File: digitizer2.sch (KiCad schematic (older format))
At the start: 4 parts, among them U1 XC7A35T, U2 FT2232H, U3 MT41K128M16, U4 ADS5403

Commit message: .
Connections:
- net labels added: ADC_DA0_N, ADC_DA0_P, ADC_DA10_N, ADC_DA10_P, ADC_DA11_N, ADC_DA11_P, ADC_DA1_N, ADC_DA1_P, ADC_DA2_N, ADC_DA2_P, ADC_DA3_N, ADC_DA3_P, ADC_DA4_N, ADC_DA4_P, ADC_DA5_N, ADC_DA5_P, ADC_DA6_N, ADC_DA6_P, ADC_DA7_N, ADC_DA7_P, ADC_DA8_N, ADC_DA8_P, ADC_DA9_N, ADC_DA9_P, ADC_DACLK_N, ADC_DACLK_P, ADC_OVRA_N, ADC_OVRA_P, ADC_SCLK, ADC_SDENB, ADC_SDIO, ADC_SDO, DRAM_A0, DRAM_A1, DRAM_A10, DRAM_A11, DRAM_A12, DRAM_A13, DRAM_A2, DRAM_A3, DRAM_A4, DRAM_A5, DRAM_A6, DRAM_A7, DRAM_A8, DRAM_A9, DRAM_BA0, DRAM_BA1, DRAM_BA2, DRAM_CAS, DRAM_CKE, DRAM_CK_N, DRAM_CK_P, DRAM_CS, DRAM_DM0, DRAM_DM1, DRAM_DQ0, DRAM_DQ1, DRAM_DQ10, DRAM_DQ11, DRAM_DQ12, DRAM_DQ13, DRAM_DQ14, DRAM_DQ15, DRAM_DQ2, DRAM_DQ3, DRAM_DQ4, DRAM_DQ5, DRAM_DQ6, DRAM_DQ7, DRAM_DQ8, DRAM_DQ9, DRAM_DQS0_N, DRAM_DQS0_P, DRAM_DQS1_N, DRAM_DQS1_P, DRAM_ODT, DRAM_RAS, DRAM_RESET, DRAM_WE, DRAM_ZQ, JTAG_TCK, JTAG_TDI, JTAG_TDO, JTAG_TMS, USB_CLKOUT, USB_D0, USB_D1, USB_D2, USB_D3, USB_D4, USB_D5, USB_D6, USB_D7, USB_OE, USB_RD, USB_RXF, USB_TXE, USB_WR
- wire segments 8 -> 18
- no-connect marks 0 -> 19
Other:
- moved on the sheet: U4

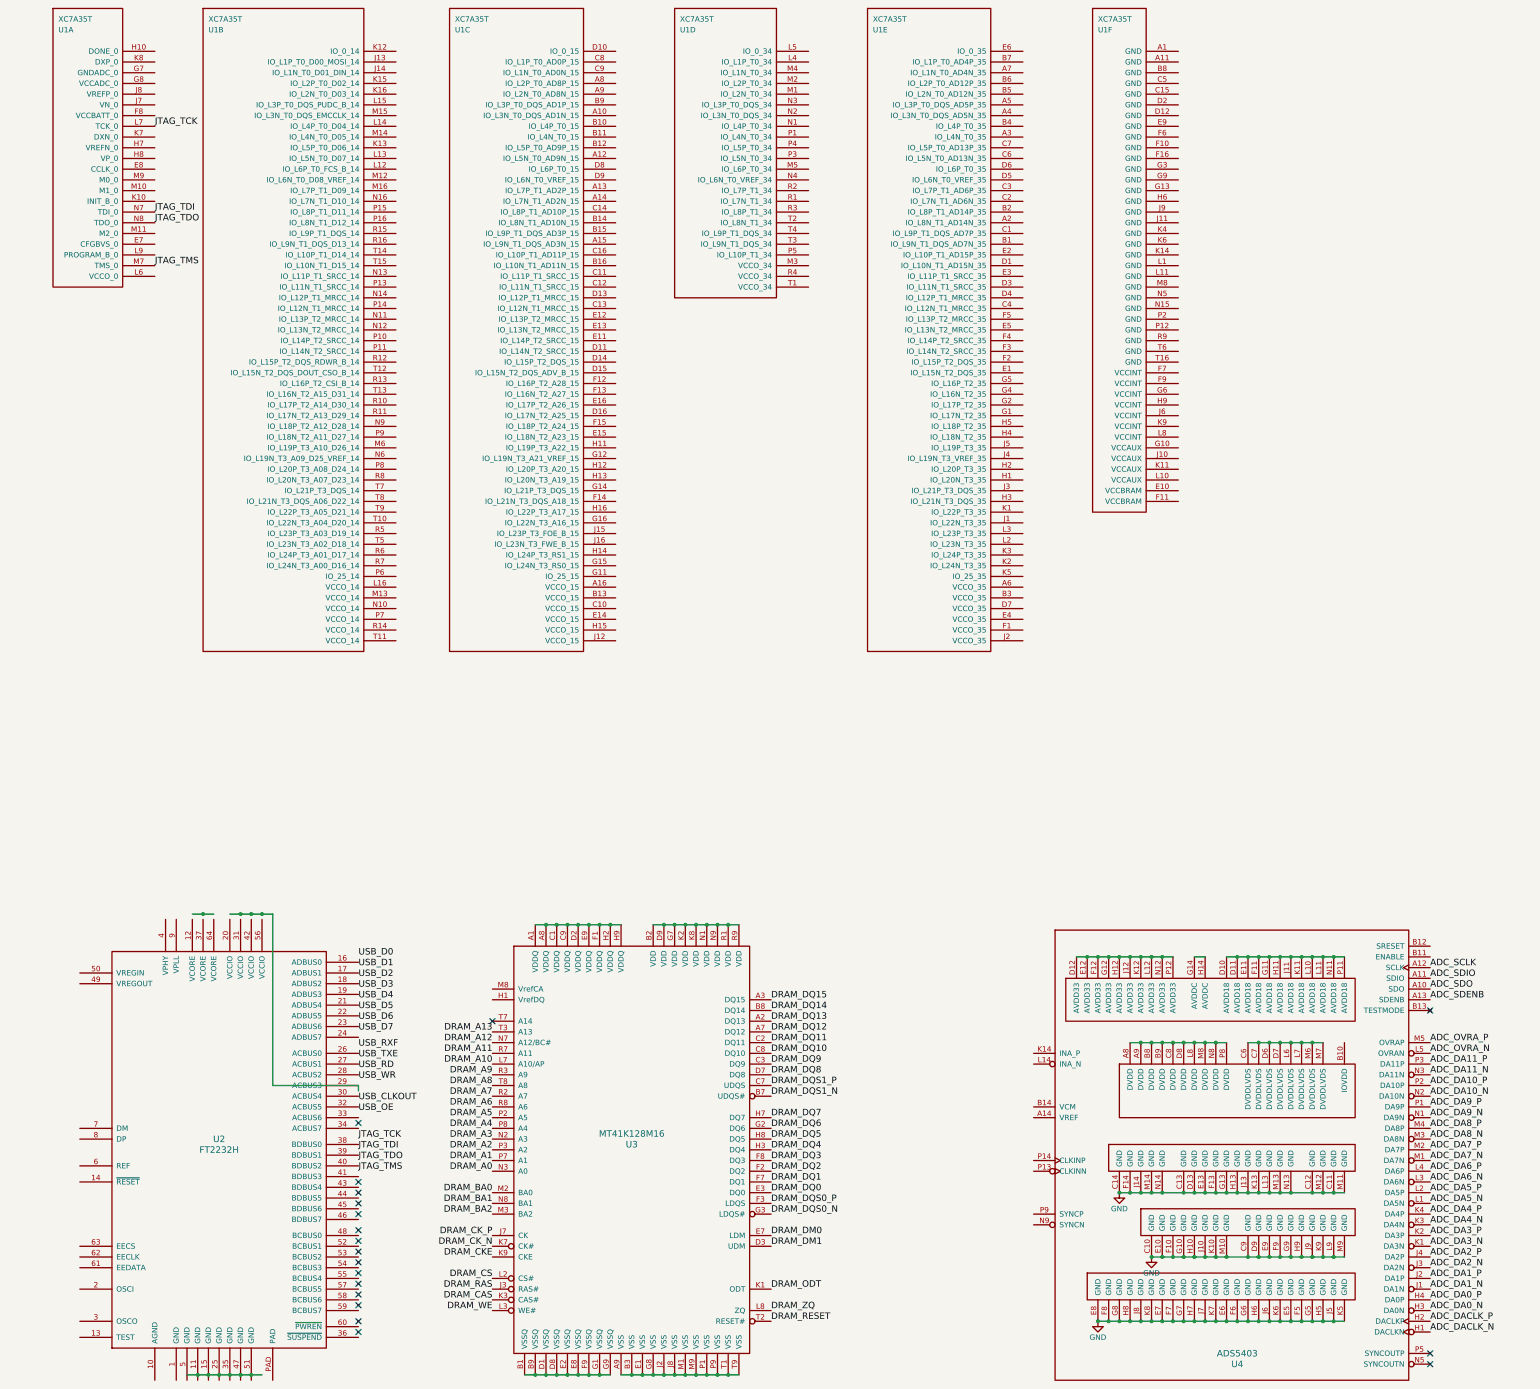
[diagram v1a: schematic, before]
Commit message: Tuned ADC DDR layout
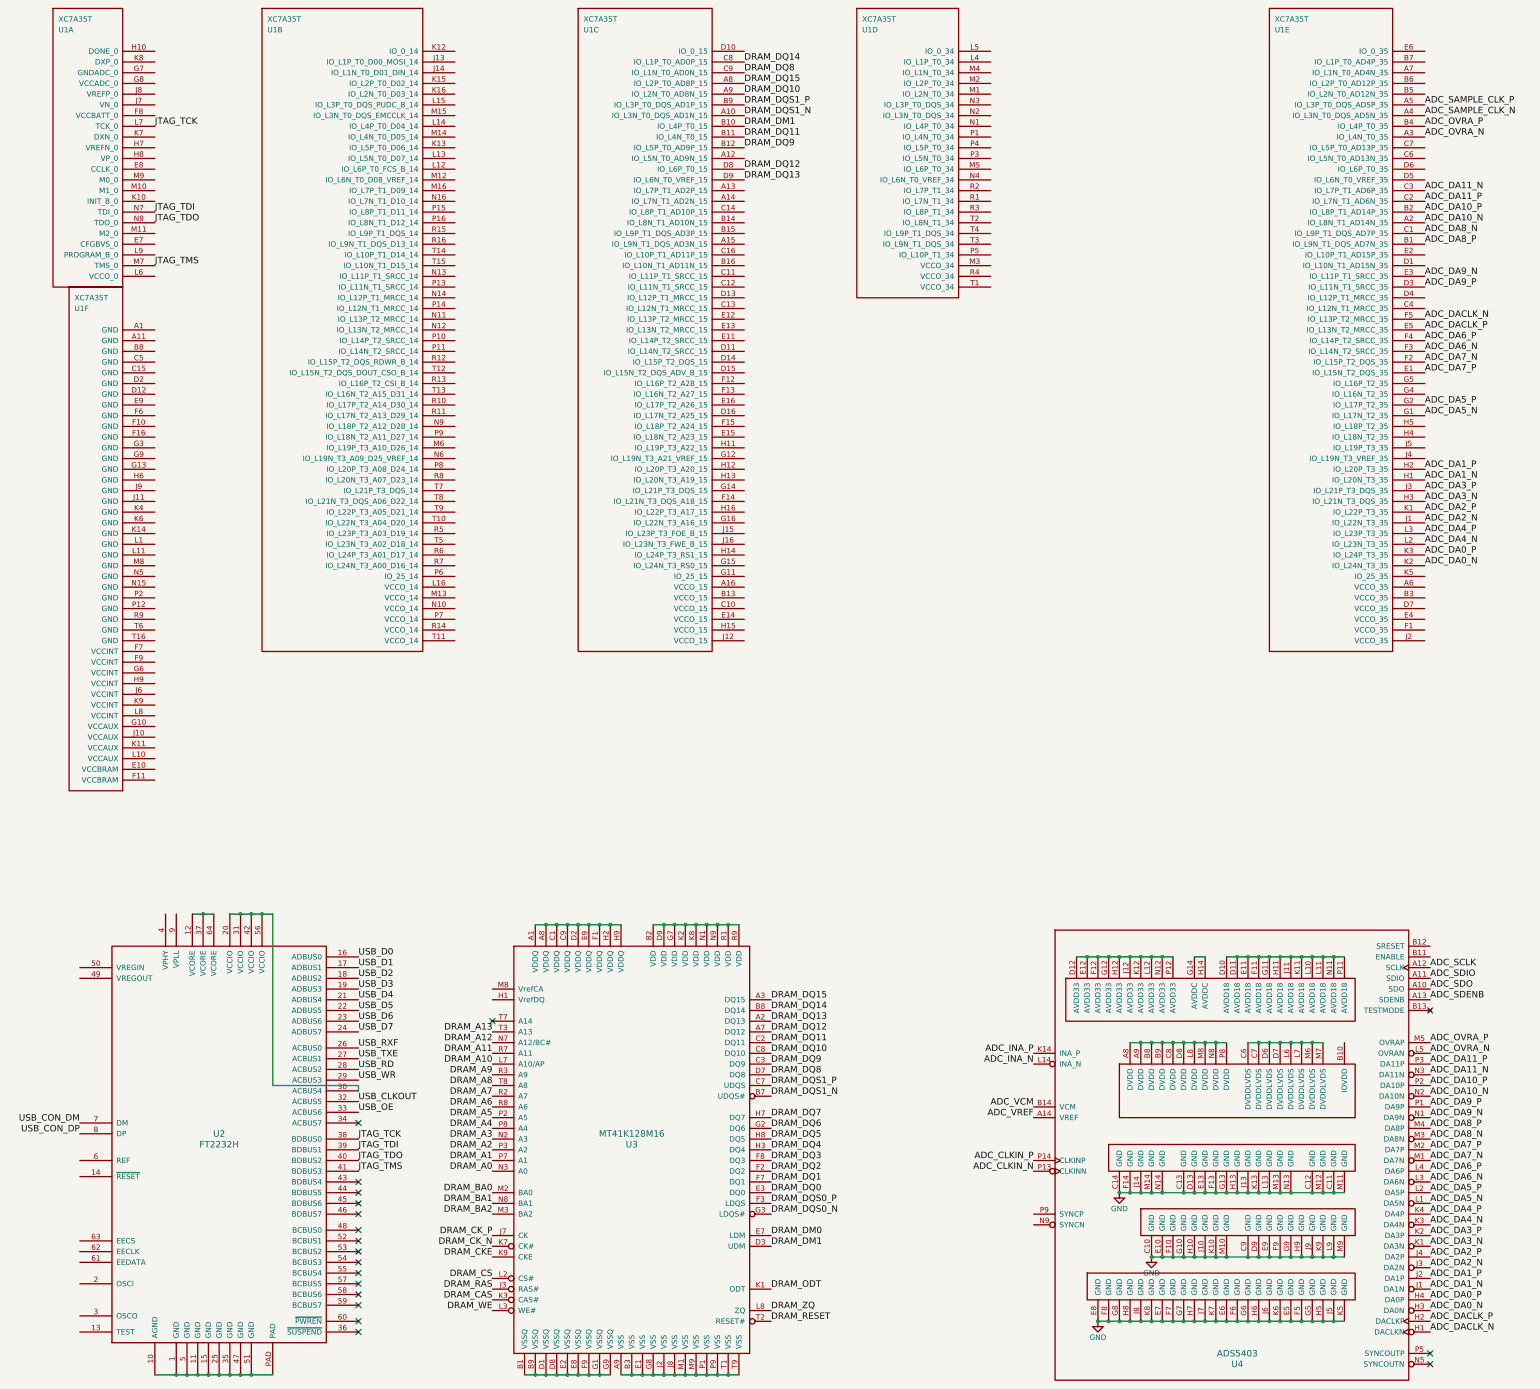
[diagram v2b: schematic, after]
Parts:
- U2: footprint (none) -> digitizer2_modules:QFN-FT2232HQ-64_pitch0.5
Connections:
- net labels added: ADC_CLKIN_N, ADC_CLKIN_P, ADC_INA_N, ADC_INA_P, ADC_SAMPLE_CLK_N, ADC_SAMPLE_CLK_P, ADC_VCM, ADC_VREF, USB_CON_DM, USB_CON_DP
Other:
- moved on the sheet: U1B, U1C, U1D, U1E, U1F, U2
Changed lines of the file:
@@
 L XC7A35T U1
 U 2 1 56D56ABF
-P 1900 800
-F 0 "U1" H 1950 900 50  0000 L CNN
-F 1 "XC7A35T" H 1950 1000 50  0000 L CNN
-F 2 "" H 1900 800 60  0000 C CNN
-F 3 "" H 1900 800 60  0000 C CNN
-	2    1900 800
+P 2450 800
+F 0 "U1" H 2500 900 50  0000 L CNN
+F 1 "XC7A35T" H 2500 1000 50  0000 L CNN
+F 2 "" H 2450 800 60  0000 C CNN
+F 3 "" H 2450 800 60  0000 C CNN
+	2    2450 800
 	1    0    0    -1
 $EndComp
@@
 L XC7A35T U1
 U 3 1 56D56B34
-P 4200 800
-F 0 "U1" H 4250 900 50  0000 L CNN
-F 1 "XC7A35T" H 4250 1000 50  0000 L CNN
-F 2 "" H 4200 800 60  0000 C CNN
-F 3 "" H 4200 800 60  0000 C CNN
-	3    4200 800
+P 5400 800
+F 0 "U1" H 5450 900 50  0000 L CNN
+F 1 "XC7A35T" H 5450 1000 50  0000 L CNN
+F 2 "" H 5400 800 60  0000 C CNN
+F 3 "" H 5400 800 60  0000 C CNN
+	3    5400 800
 	1    0    0    -1
 $EndComp
@@
 L XC7A35T U1
 U 4 1 56D56B7F
-P 6300 800
-F 0 "U1" H 6350 900 50  0000 L CNN
-F 1 "XC7A35T" H 6350 1000 50  0000 L CNN
-F 2 "" H 6300 800 60  0000 C CNN
-F 3 "" H 6300 800 60  0000 C CNN
-	4    6300 800
+P 8000 800
+F 0 "U1" H 8050 900 50  0000 L CNN
+F 1 "XC7A35T" H 8050 1000 50  0000 L CNN
+F 2 "" H 8000 800 60  0000 C CNN
+F 3 "" H 8000 800 60  0000 C CNN
+	4    8000 800
 	1    0    0    -1
 $EndComp
@@
 L XC7A35T U1
 U 5 1 56D56C00
-P 8100 800
-F 0 "U1" H 8150 900 50  0000 L CNN
-F 1 "XC7A35T" H 8150 1000 50  0000 L CNN
-F 2 "" H 8100 800 60  0000 C CNN
-F 3 "" H 8100 800 60  0000 C CNN
-	5    8100 800
+P 11850 800
+F 0 "U1" H 11900 900 50  0000 L CNN
+F 1 "XC7A35T" H 11900 1000 50  0000 L CNN
+F 2 "" H 11850 800 60  0000 C CNN
+F 3 "" H 11850 800 60  0000 C CNN
+	5    11850 800
 	1    0    0    -1
 $EndComp
@@
 L XC7A35T U1
 U 6 1 56D56C67
-P 10200 800
-F 0 "U1" H 10250 900 50  0000 L CNN
-F 1 "XC7A35T" H 10250 1000 50  0000 L CNN
-F 2 "" H 10200 800 60  0000 C CNN
-F 3 "" H 10200 800 60  0000 C CNN
-	6    10200 800
+P 650 3400
+F 0 "U1" H 700 3500 50  0000 L CNN
+F 1 "XC7A35T" H 700 3600 50  0000 L CNN
+F 2 "" H 650 3400 60  0000 C CNN
+F 3 "" H 650 3400 60  0000 C CNN
+	6    650  3400
 	1    0    0    -1
 $EndComp
@@
 L FT2232H U2
 U 1 1 56D58984
-P 2050 11100
-F 0 "U2" H 2050 11150 60  0000 C CNN
-F 1 "FT2232H" H 2050 11050 60  0000 C CNN
-F 2 "" H 2050 11100 60  0000 C CNN
-F 3 "" H 2050 11100 60  0000 C CNN
-	1    2050 11100
+P 2050 11050
+F 0 "U2" H 2050 11100 60  0000 C CNN
+F 1 "FT2232H" H 2050 11000 60  0000 C CNN
+F 2 "digitizer2_modules:QFN-FT2232HQ-64_pitch0.5" H 2050 11050 60  0001 C CNN
+F 3 "" H 2050 11050 60  0000 C CNN
+	1    2050 11050
 	1    0    0    -1
 $EndComp
@@
 $EndComp
 $Comp
-L GND #PWR?
+L GND #PWR01
 U 1 1 56D761B1
 P 10450 11550
-F 0 "#PWR?" H 10450 11300 50  0001 C CNN
+F 0 "#PWR01" H 10450 11300 50  0001 C CNN
 F 1 "GND" H 10450 11400 50  0000 C CNN
 F 2 "" H 10450 11550 50  0000 C CNN
@@
 $EndComp
 $Comp
-L GND #PWR?
+L GND #PWR02
 U 1 1 56D76204
 P 10750 12150
-F 0 "#PWR?" H 10750 11900 50  0001 C CNN
+F 0 "#PWR02" H 10750 11900 50  0001 C CNN
 F 1 "GND" H 10750 12000 50  0000 C CNN
 F 2 "" H 10750 12150 50  0000 C CNN
@@
 $EndComp
 $Comp
-L GND #PWR?
+L GND #PWR03
 U 1 1 56D764BB
 P 10250 12750
-F 0 "#PWR?" H 10250 12500 50  0001 C CNN
+F 0 "#PWR03" H 10250 12500 50  0001 C CNN
 F 1 "GND" H 10250 12600 50  0000 C CNN
 F 2 "" H 10250 12750 50  0000 C CNN
@@
 	1800 8950 2000 8950
 Connection ~ 1900 8950
-Wire Wire Line
-	1750 13250 2450 13250
 Connection ~ 2350 13250
 Connection ~ 2250 13250
@@
 Text Label 1450 2500 0    60   ~ 0
 JTAG_TDO
+Wire Wire Line
+	1450 13250 2550 13250
+Connection ~ 1750 13250
+Connection ~ 1650 13250
+Text Label 750  10900 2    60   ~ 0
+USB_CON_DM
+Text Label 750  11000 2    60   ~ 0
+USB_CON_DP
+Text Label 9650 10250 2    60   ~ 0
+ADC_INA_P
+Text Label 9650 10350 2    60   ~ 0
+ADC_INA_N
+Text Label 9650 10750 2    60   ~ 0
+ADC_VCM
+Text Label 9650 10850 2    60   ~ 0
+ADC_VREF
+Text Label 9650 11250 2    60   ~ 0
+ADC_CLKIN_P
+Text Label 9650 11350 2    60   ~ 0
+ADC_CLKIN_N
+Text Label 6950 1400 0    60   ~ 0
+DRAM_DQS1_P
+Text Label 6950 1500 0    60   ~ 0
+DRAM_DQS1_N
+Text Label 6950 2000 0    60   ~ 0
+DRAM_DQ12
+Text Label 6950 1000 0    60   ~ 0
+DRAM_DQ14
+Text Label 6950 1200 0    60   ~ 0
+DRAM_DQ15
+Text Label 6950 2100 0    60   ~ 0
+DRAM_DQ13
+Text Label 6950 1100 0    60   ~ 0
+DRAM_DQ8
+Text Label 6950 1300 0    60   ~ 0
+DRAM_DQ10
+Text Label 6950 1600 0    60   ~ 0
+DRAM_DM1
+Text Label 6950 1700 0    60   ~ 0
+DRAM_DQ11
+Text Label 6950 1800 0    60   ~ 0
+DRAM_DQ9
+Text Label 13300 3400 0    60   ~ 0
+ADC_DACLK_N
+Text Label 13300 3500 0    60   ~ 0
+ADC_DACLK_P
+Text Label 13300 5400 0    60   ~ 0
+ADC_DA4_P
+Text Label 13300 5500 0    60   ~ 0
+ADC_DA4_N
+Text Label 13300 5600 0    60   ~ 0
+ADC_DA0_P
+Text Label 13300 5700 0    60   ~ 0
+ADC_DA0_N
+Text Label 13300 5200 0    60   ~ 0
+ADC_DA2_P
+Text Label 13300 5300 0    60   ~ 0
+ADC_DA2_N
+Text Label 13300 5000 0    60   ~ 0
+ADC_DA3_P
+Text Label 13300 5100 0    60   ~ 0
+ADC_DA3_N
+Text Label 13300 4800 0    60   ~ 0
+ADC_DA1_P
+Text Label 13300 4900 0    60   ~ 0
+ADC_DA1_N
+Text Label 13300 4300 0    60   ~ 0
+ADC_DA5_N
+Text Label 13300 4200 0    60   ~ 0
+ADC_DA5_P
+Text Label 13300 3900 0    60   ~ 0
+ADC_DA7_P
+Text Label 13300 3800 0    60   ~ 0
+ADC_DA7_N
+Text Label 13300 3700 0    60   ~ 0
+ADC_DA6_N
+Text Label 13300 3600 0    60   ~ 0
+ADC_DA6_P
+Text Label 13300 3000 0    60   ~ 0
+ADC_DA9_N
+Text Label 13300 3100 0    60   ~ 0
+ADC_DA9_P
+Text Label 13300 2700 0    60   ~ 0
+ADC_DA8_P
+Text Label 13300 2600 0    60   ~ 0
+ADC_DA8_N
+Text Label 13300 2300 0    60   ~ 0
+ADC_DA11_P
+Text Label 13300 2200 0    60   ~ 0
+ADC_DA11_N
+Text Label 13300 2400 0    60   ~ 0
+ADC_DA10_P
+Text Label 13300 2500 0    60   ~ 0
+ADC_DA10_N
+Text Label 13300 1700 0    60   ~ 0
+ADC_OVRA_N
+Text Label 13300 1600 0    60   ~ 0
+ADC_OVRA_P
+Text Label 13300 1400 0    60   ~ 0
+ADC_SAMPLE_CLK_P
+Text Label 13300 1500 0    60   ~ 0
+ADC_SAMPLE_CLK_N
 $EndSCHEMATC

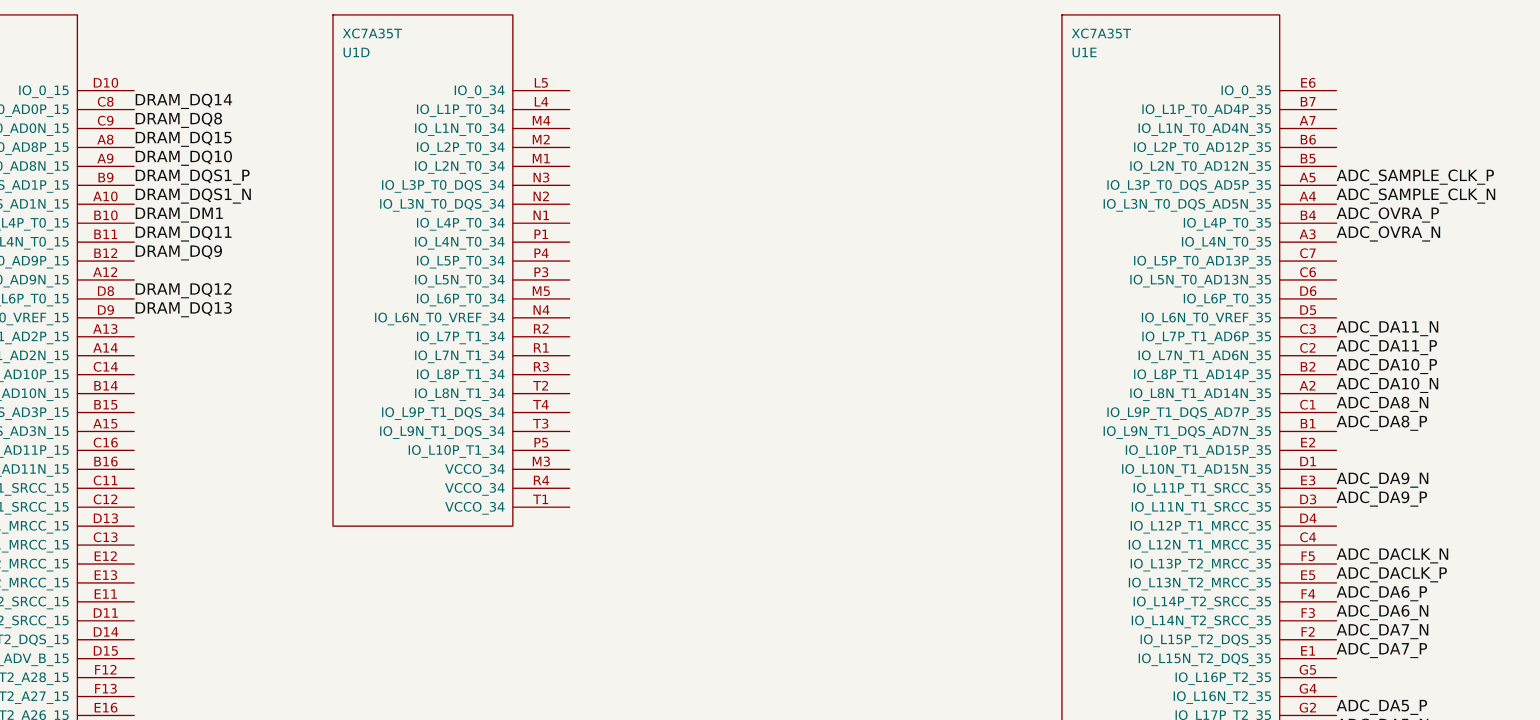
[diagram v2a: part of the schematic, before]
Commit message: Changed LVDS layout. Try new DRAM position.
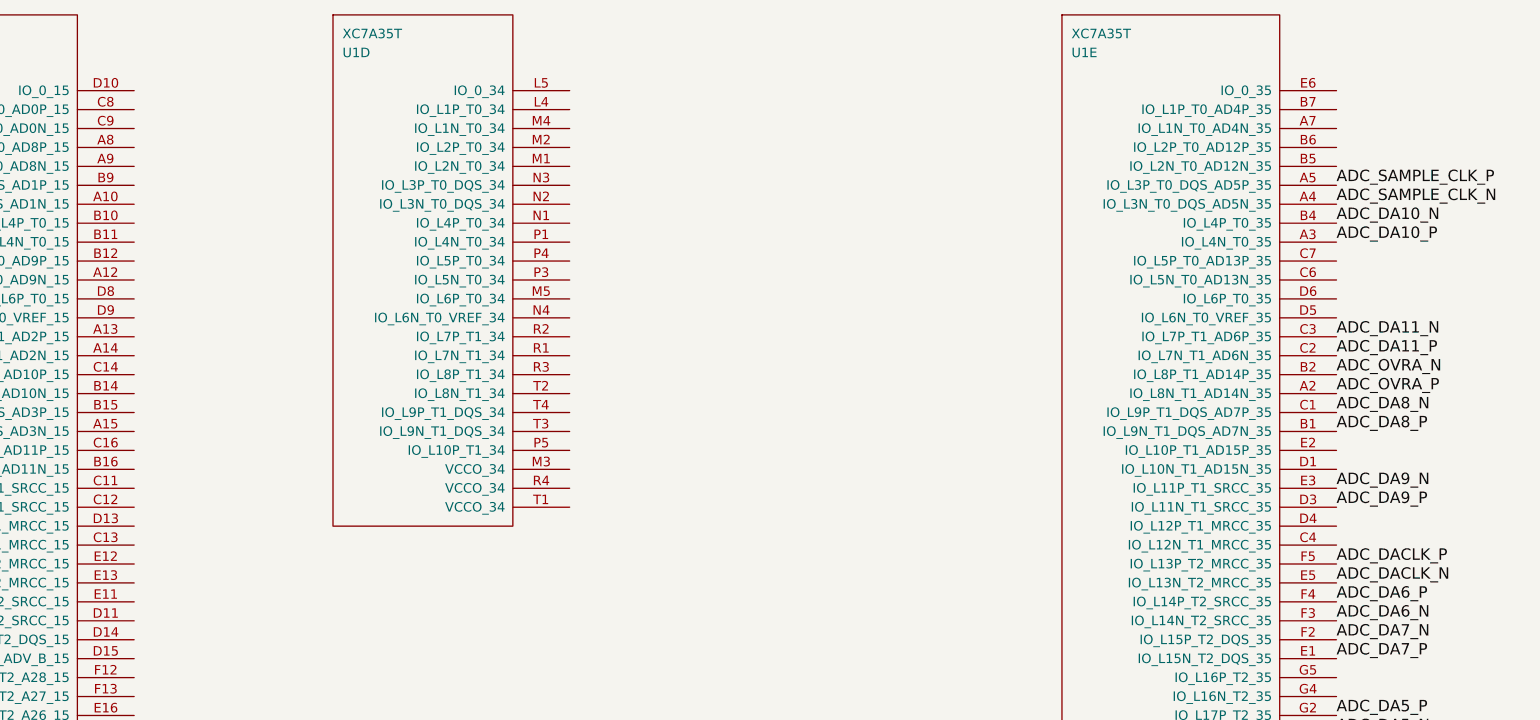
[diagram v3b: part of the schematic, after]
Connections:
- net ADC_DA10_N: now also U1.B4 (IO_L4P_T0_35); no longer U1.A2 (IO_L8N_T1_AD14N_35)
- net ADC_DA10_P: now also U1.A3 (IO_L4N_T0_35); no longer U1.B2 (IO_L8P_T1_AD14P_35)
- net ADC_DACLK_N: now also U1.E5 (IO_L13N_T2_MRCC_35); no longer U1.F5 (IO_L13P_T2_MRCC_35)
- net ADC_DACLK_P: now also U1.F5 (IO_L13P_T2_MRCC_35); no longer U1.E5 (IO_L13N_T2_MRCC_35)
- net ADC_OVRA_N: now also U1.B2 (IO_L8P_T1_AD14P_35); no longer U1.A3 (IO_L4N_T0_35)
- net ADC_OVRA_P: now also U1.A2 (IO_L8N_T1_AD14N_35); no longer U1.B4 (IO_L4P_T0_35)
- net DRAM_DM1: no longer U1.B10 (IO_L4P_T0_15)
- net DRAM_DQ10: no longer U1.A9 (IO_L2N_T0_AD8N_15)
- net DRAM_DQ11: no longer U1.B11 (IO_L4N_T0_15)
- net DRAM_DQ12: no longer U1.D8 (IO_L6P_T0_15)
- net DRAM_DQ13: no longer U1.D9 (IO_L6N_T0_VREF_15)
- net DRAM_DQ14: no longer U1.C8 (IO_L1P_T0_AD0P_15)
- net DRAM_DQ15: no longer U1.A8 (IO_L2P_T0_AD8P_15)
- net DRAM_DQ8: no longer U1.C9 (IO_L1N_T0_AD0N_15)
- net DRAM_DQ9: no longer U1.B12 (IO_L5P_T0_AD9P_15)
- net DRAM_DQS1_N: no longer U1.A10 (IO_L3N_T0_DQS_AD1N_15)
- net DRAM_DQS1_P: no longer U1.B9 (IO_L3P_T0_DQS_AD1P_15)
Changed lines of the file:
@@
 Text Label 9650 11350 2    60   ~ 0
 ADC_CLKIN_N
-Text Label 6950 1400 0    60   ~ 0
-DRAM_DQS1_P
-Text Label 6950 1500 0    60   ~ 0
-DRAM_DQS1_N
-Text Label 6950 2000 0    60   ~ 0
-DRAM_DQ12
-Text Label 6950 1000 0    60   ~ 0
-DRAM_DQ14
-Text Label 6950 1200 0    60   ~ 0
-DRAM_DQ15
-Text Label 6950 2100 0    60   ~ 0
-DRAM_DQ13
-Text Label 6950 1100 0    60   ~ 0
-DRAM_DQ8
-Text Label 6950 1300 0    60   ~ 0
-DRAM_DQ10
-Text Label 6950 1600 0    60   ~ 0
-DRAM_DM1
-Text Label 6950 1700 0    60   ~ 0
-DRAM_DQ11
-Text Label 6950 1800 0    60   ~ 0
-DRAM_DQ9
+Text Label 13300 3500 0    60   ~ 0
+ADC_DACLK_N
 Text Label 13300 3400 0    60   ~ 0
-ADC_DACLK_N
-Text Label 13300 3500 0    60   ~ 0
 ADC_DACLK_P
 Text Label 13300 5400 0    60   ~ 0
@@
 Text Label 13300 2200 0    60   ~ 0
 ADC_DA11_N
+Text Label 13300 1700 0    60   ~ 0
+ADC_DA10_P
+Text Label 13300 1600 0    60   ~ 0
+ADC_DA10_N
 Text Label 13300 2400 0    60   ~ 0
-ADC_DA10_P
+ADC_OVRA_N
 Text Label 13300 2500 0    60   ~ 0
-ADC_DA10_N
-Text Label 13300 1700 0    60   ~ 0
-ADC_OVRA_N
-Text Label 13300 1600 0    60   ~ 0
 ADC_OVRA_P
 Text Label 13300 1400 0    60   ~ 0
